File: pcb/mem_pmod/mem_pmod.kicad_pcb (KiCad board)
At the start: 4 copper layers, 11 parts

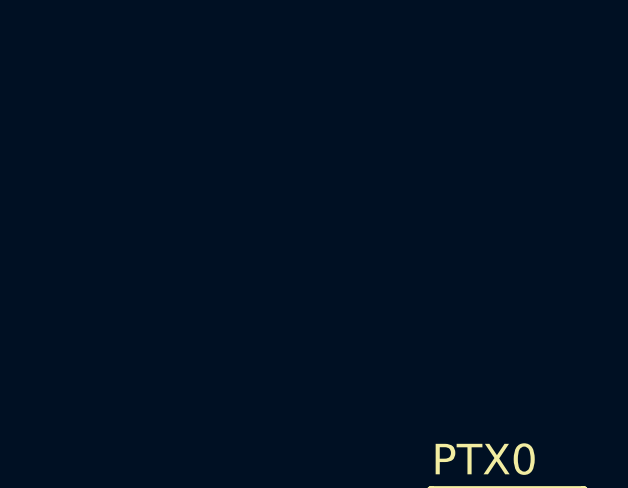
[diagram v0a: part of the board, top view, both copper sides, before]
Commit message: continue editing schematic
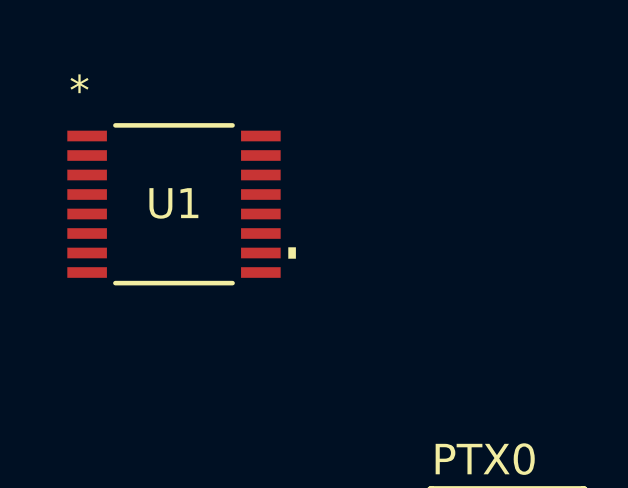
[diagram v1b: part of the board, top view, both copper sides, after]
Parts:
- added U1: 74ACT139MTCX, footprints:TSSOP16_5X4P5_ONS, F.Cu at (3.89, 2.83)

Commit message: Replacing components in schematic due to prop delay
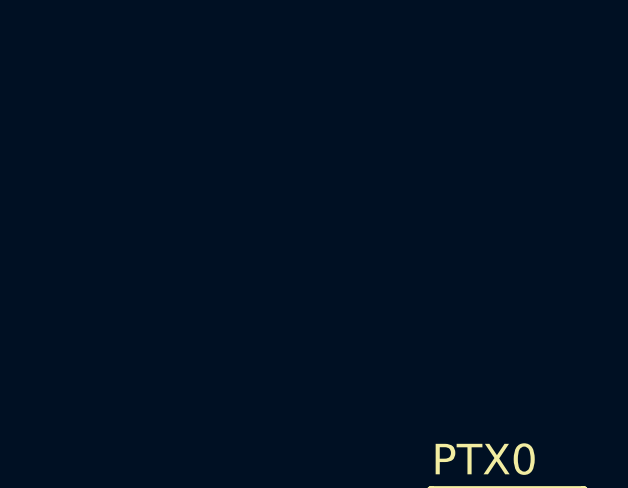
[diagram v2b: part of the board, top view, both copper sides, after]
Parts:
- removed U1: 74ACT139MTCX, footprints:TSSOP16_5X4P5_ONS
